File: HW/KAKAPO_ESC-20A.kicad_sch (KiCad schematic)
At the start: 30 parts

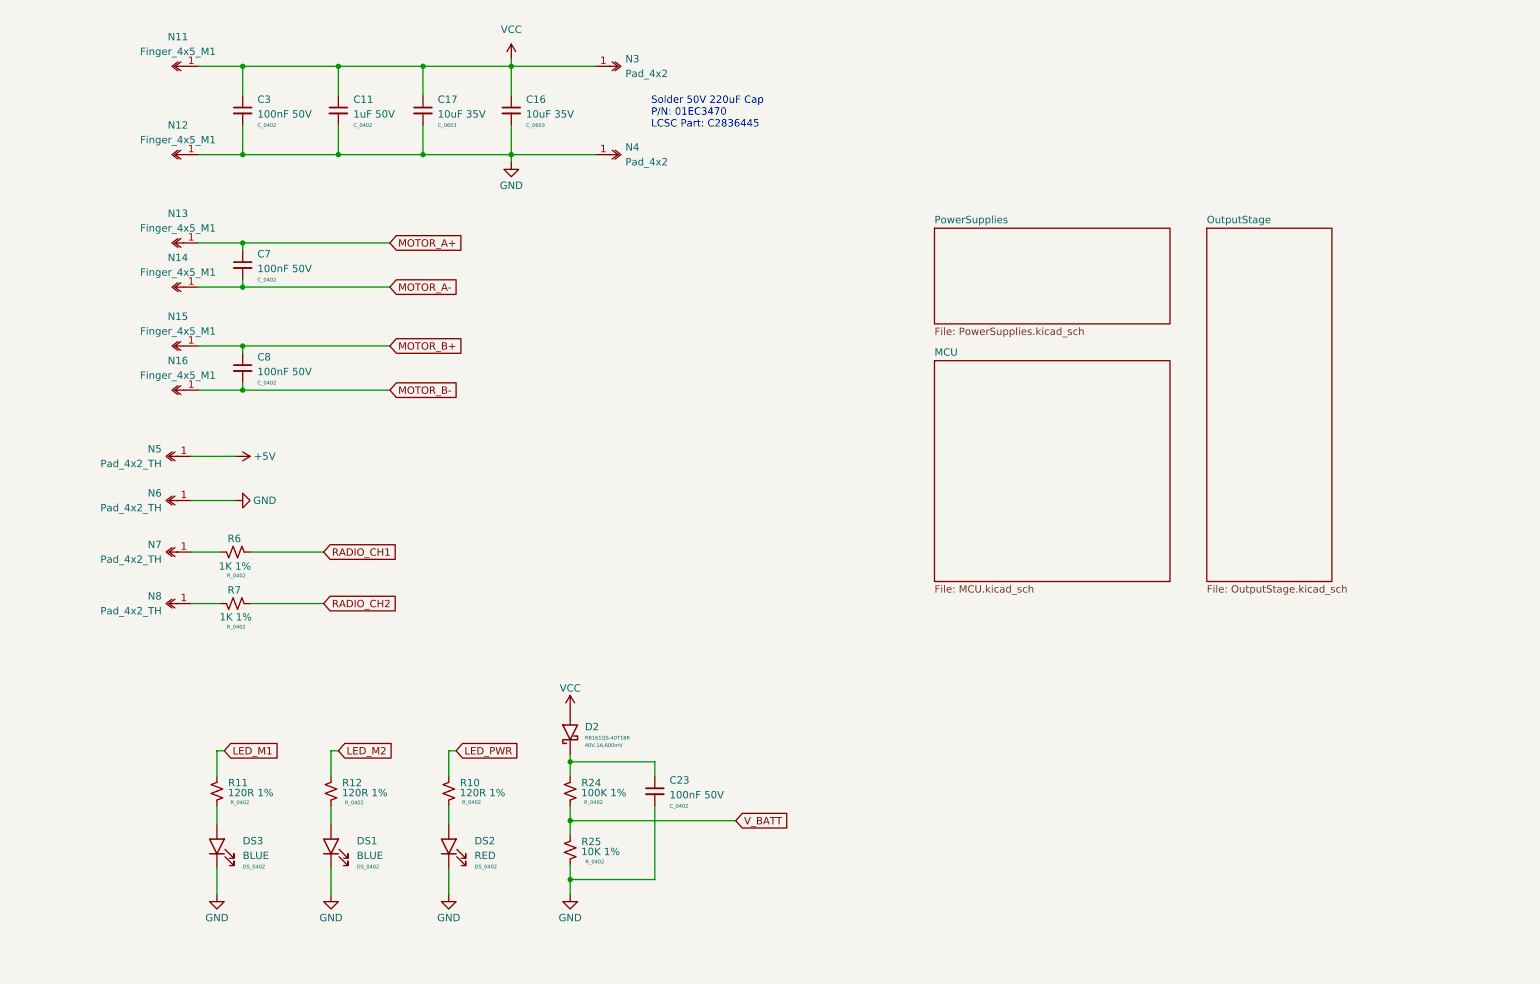
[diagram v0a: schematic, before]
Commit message: WIP - Layout XT30/PCB Finger Positions
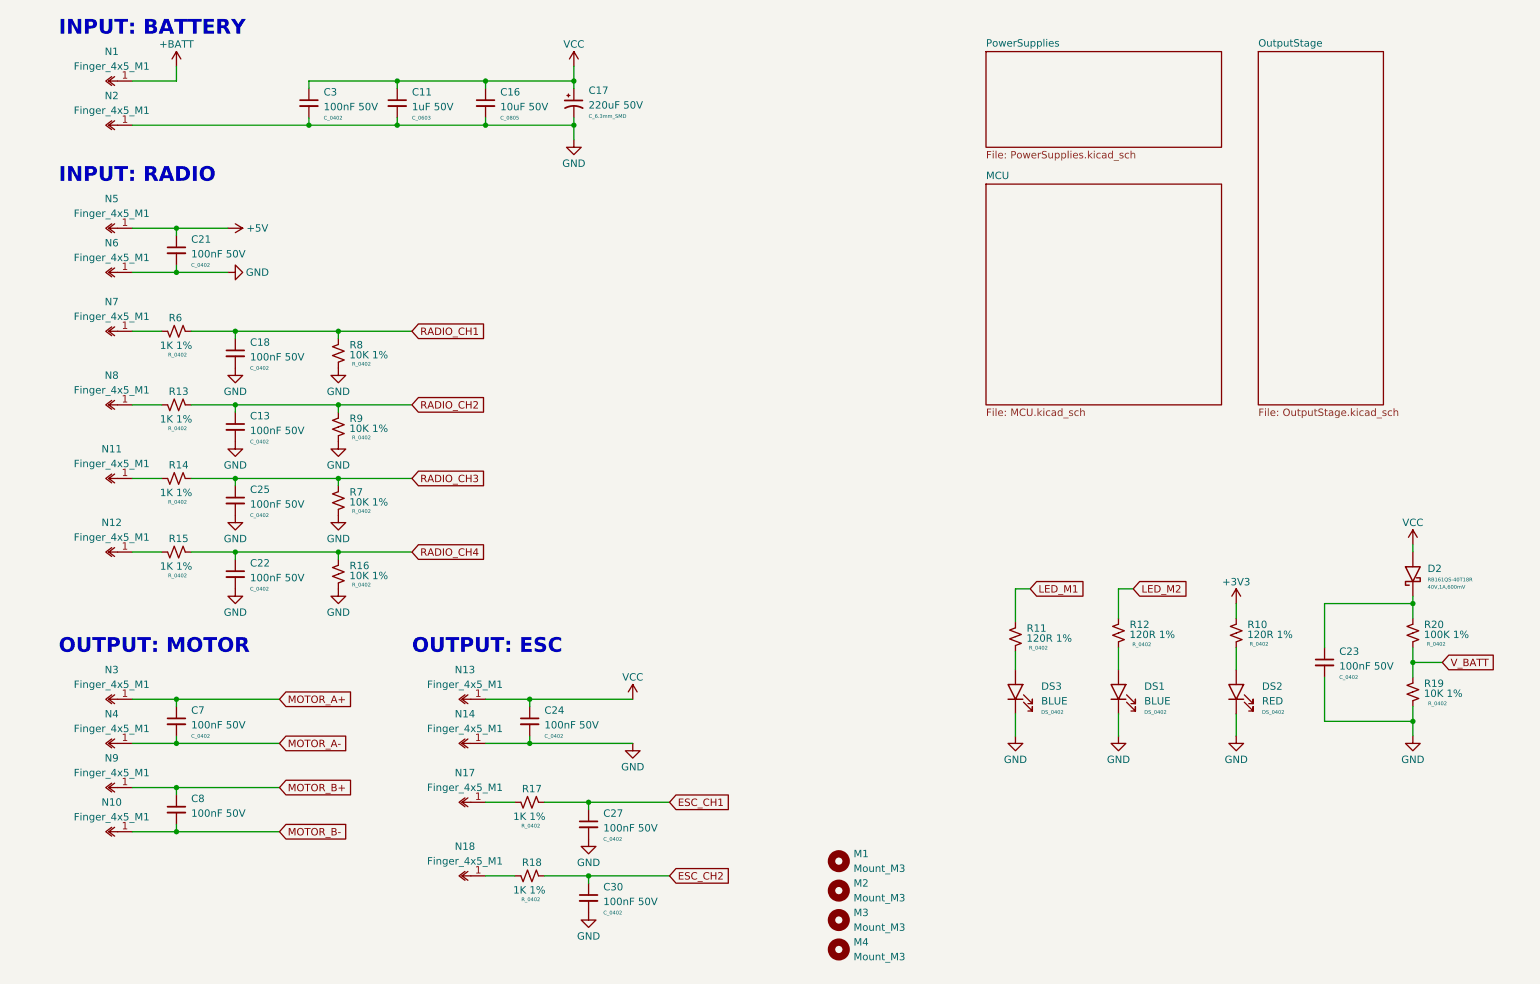
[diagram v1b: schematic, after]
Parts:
- removed C11: 1uF 50V, C_Capacitor:C_0402, symbol C_Capacitor:C_0402
- removed C17: 10uF 35V, C_Capacitor:C_0603, symbol C_Capacitor:C_0805
- removed N15, N16: Finger_4x5_M1, N_NonPart:Finger_4x5_M1, symbol N_NonPart:Finger_4x5_M1
- removed N3, N4: Pad_4x2, N_NonPart:Pad_4x2, symbol N_NonPart:Pad_4x2
- removed N5, N6, N7, N8: Pad_4x2_TH, N_NonPart:Pad_4x2, symbol N_NonPart:Pad_4x2_TH
- removed R24: 100K 1%, R_Resistor:R_0402, symbol R_Resistor:R_0402
- removed R25: 10K 1%, R_Resistor:R_0402, symbol R_Resistor:R_0402
- added C11: 1uF 50V, C_Capacitor:C_0603, symbol C_Capacitor:C_0805
- added C13, C18, C21, C22, C24, C25, C27, C30: 100nF 50V, C_Capacitor:C_0402, symbol C_Capacitor:C_0402
- added C17: 220uF 50V, C_Capacitor:C_6.3mm_SMD, symbol C_Capacitor:C_6.3mm_SMD
- added M1, M2, M3, M4: Mount_M3, M_Mechanical:Mount_M3, symbol M_Mechanical:Mount_M3
- added N1, N10, N17, N18, N2, N3, N4, N5, N6, N7, N8, N9: Finger_4x5_M1, N_NonPart:Finger_4x5_M1, symbol N_NonPart:Finger_4x5_M1
- added R13, R14, R15, R17, R18: 1K 1%, R_Resistor:R_0402, symbol R_Resistor:R_0402
- added R16, R19, R8, R9: 10K 1%, R_Resistor:R_0402, symbol R_Resistor:R_0402
- added R20: 100K 1%, R_Resistor:R_0402, symbol R_Resistor:R_0402
- C16: value 10uF 35V -> 10uF 50V; footprint C_Capacitor:C_0603 -> C_Capacitor:C_0805; LCSC Part C194427 -> (none); Size C_0603 -> C_0805
- R7: value 1K 1% -> 10K 1%; LCSC Part C2935237 -> C309549
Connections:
- net +5V: now also C21.1, N5.1
- net GND: now also N14.1, R7.2, C11.2, C13.2, C17.2, C18.2, C21.2, C22.2, C24.2, C25.2, C27.2, C30.2, N2.1, N6.1, R16.2, R19.2, R8.2, R9.2; no longer N12.1
- net MOTOR_A+: now also N3.1; no longer N13.1
- net MOTOR_A-: now also N4.1; no longer N14.1
- net MOTOR_B+: now also N9.1
- net MOTOR_B-: now also N10.1
- net RADIO_CH1: now also C18.1, R8.1
- net RADIO_CH2: now also C13.1, R13.2, R9.1; no longer R7.2
- net VCC: now also N13.1, C11.1, C17.1, C24.1; no longer N11.1
- net V_BATT: now also R19.1, R20.2
- net RADIO_CH3: now reaches R7.1
- net RADIO_CH3: now also C25.1, R14.2
- net at C23.1, D2.1: now also R20.1
- net at R6.1: now also N7.1
- net LED_PWR renamed +3V3
- new net: N17.1, R17.1
- new net: N12.1, R15.1
- new net: N8.1, R13.1
- new net: N11.1, R14.1
- new net: N18.1, R18.1
- new net +BATT: N1.1
- new net ESC_CH1: C27.1, R17.2
- new net ESC_CH2: C30.1, R18.2
- new net RADIO_CH4: C22.1, R15.2, R16.1
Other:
- note added: "INPUT: BATTERY"
- note added: "INPUT: RADIO"
- note added: "OUTPUT: ESC"
- note added: "OUTPUT: MOTOR"
- note removed: "Solder 50V 220uF Cap P/N: 01EC3470 LCSC Part: C2836445"
- title: WEKA ESC - 20A -> KAKAPO ESC - 20A
- moved on the sheet: DS3, R11, R12

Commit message: WIP - Layout Motor Drivers + Buck Circuit
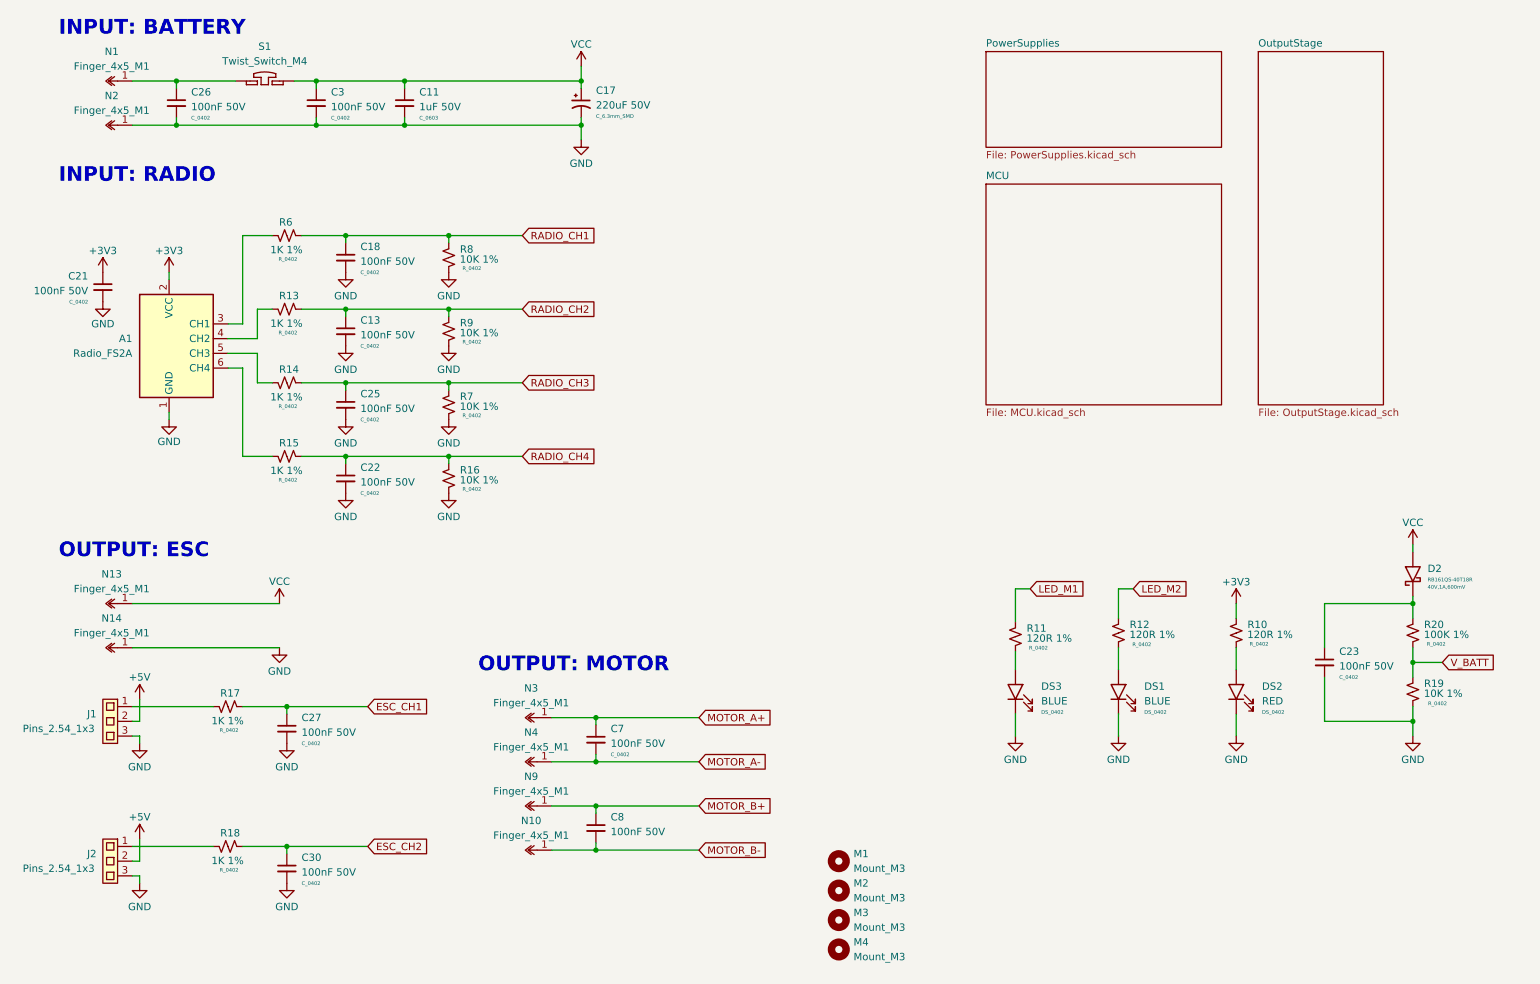
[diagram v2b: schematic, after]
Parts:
- removed C16: 10uF 50V, C_Capacitor:C_0805, symbol C_Capacitor:C_0805
- removed C24: 100nF 50V, C_Capacitor:C_0402, symbol C_Capacitor:C_0402
- removed N11, N12, N17, N18, N5, N6, N7, N8: Finger_4x5_M1, N_NonPart:Finger_4x5_M1, symbol N_NonPart:Finger_4x5_M1
- added A1: Radio_FS2A, A_Assembly:Radio_FS2A, symbol A_Assembly:Radio_FS2A
- added C26: 100nF 50V, C_Capacitor:C_0402, symbol C_Capacitor:C_0402
- added J1, J2: Pins_2.54_1x3, J_Connector:Pins-2.54-1x3, symbol J_Connector:Pins_2.54_1x3
- added S1: Twist_Switch_M4, CombatParts:Twist_Switch_M4, symbol CombatParts:Twist_Switch_M4
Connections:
- net +3V3: now also C21.1, A1.2 (VCC)
- net +5V: now also J1.2, J2.2; no longer C21.1
- net GND: now also A1.1 (GND), C26.2, J1.3, J2.3
- net VCC: now also S1.2
- net at R6.1: now also A1.3 (CH1)
- net at R17.1: now also J1.1
- net at R15.1: now also A1.6 (CH4)
- net at R13.1: now also A1.4 (CH2)
- net at R14.1: now also A1.5 (CH3)
- net at R18.1: now also J2.1
- net +BATT: no longer names the net of N1.1
- net +BATT: now also C26.1, S1.1
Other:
- moved on the sheet: C11, C13, C17, C18, C22, C25, C27, C3, C30, C7, C8, N10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

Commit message: WIP - Continue Tracking MCU
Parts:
- removed C21: 100nF 50V, C_Capacitor:C_0402, symbol C_Capacitor:C_0402
- added C10: 100nF 50V, C_Capacitor:C_0402, symbol C_Capacitor:C_0402
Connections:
- net GND: now also C10.2
- net VCC: now also C10.1
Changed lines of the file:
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@@
   (junction (at 62.23 170.18) (diameter 0) (color 0 0 0 0)
   )
+  (junction (at 43.18 135.89) (diameter 0) (color 0 0 0 0)
+  )
   (junction (at 90.17 90.17) (diameter 0) (color 0 0 0 0)
   )
@@
   (junction (at 72.39 102.87) (diameter 0) (color 0 0 0 0)
   )
+  (junction (at 43.18 128.27) (diameter 0) (color 0 0 0 0)
+  )
   (junction (at 256.54 148.59) (diameter 0) (color 0 0 0 0)
   )
@@
     (stroke (width 0) (type default))
   )
+  (wire (pts (xy 43.18 134.62) (xy 43.18 135.89))
+    (stroke (width 0) (type default))
+  )
   (wire (pts (xy 62.23 171.45) (xy 62.23 170.18))
     (stroke (width 0) (type default))
@@
     (stroke (width 0) (type default))
   )
+  (wire (pts (xy 43.18 128.27) (xy 43.18 129.54))
+    (stroke (width 0) (type default))
+  )
   (wire (pts (xy 54.61 64.77) (xy 59.69 64.77))
     (stroke (width 0) (type default))
@@
     (stroke (width 0) (type default))
   )
-  (wire (pts (xy 35.56 135.89) (xy 60.96 135.89))
+  (wire (pts (xy 35.56 135.89) (xy 43.18 135.89))
     (stroke (width 0) (type default))
   )
@@
     (stroke (width 0) (type default))
   )
+  (wire (pts (xy 43.18 135.89) (xy 60.96 135.89))
+    (stroke (width 0) (type default))
+  )
   (wire (pts (xy 107.95 170.815) (xy 115.57 170.815))
     (stroke (width 0) (type default))
@@
     (stroke (width 0) (type default))
   )
-  (wire (pts (xy 35.56 128.27) (xy 60.96 128.27))
+  (wire (pts (xy 35.56 128.27) (xy 43.18 128.27))
     (stroke (width 0) (type default))
   )
@@
     (stroke (width 0) (type default))
   )
+  (wire (pts (xy 43.18 128.27) (xy 60.96 128.27))
+    (stroke (width 0) (type default))
+  )
   (wire (pts (xy 72.39 77.47) (xy 90.17 77.47))
     (stroke (width 0) (type default))
@@
     )
   )
-  (symbol (lib_id "C_Capacitor:C_0402") (at 30.48 73.66 0) (mirror y) (unit 1)
-    (in_bom yes) (on_board yes) (dnp no)
-    (property "Reference" "C21" (at 27.94 71.7613 0)
-      (effects (font (size 1.27 1.27)) (justify left))
-    )
-    (property "Value" "100nF 50V" (at 27.94 74.3013 0)
-      (effects (font (size 1.27 1.27)) (justify left))
-    )
-    (property "Footprint" "C_Capacitor:C_0402" (at 33.655 73.66 90)
-      (effects (font (size 1.27 1.27)) hide)
-    )
-    (property "Datasheet" "" (at 27.94 71.12 0)
-      (effects (font (size 1.27 1.27)) hide)
-    )
-    (property "Size" "C_0402" (at 27.94 76.2063 0)
-      (effects (font (size 0.635 0.635)) (justify left))
-    )
-    (property "LCSC Part" "C105882" (at 30.48 73.66 0)
-      (effects (font (size 1.27 1.27)) hide)
-    )
-    (pin "1")
-    (pin "2")
-    (instances
-      (project "KAKAPO_ESC-20A"
-        (path "/e63e39d7-6ac0-4ffd-8aa3-1841a4541b55"
-          (reference "C21") (unit 1)
-        )
-      )
-    )
-  )
   (symbol (lib_id "R_Resistor:R_0402") (at 205.74 133.35 0) (mirror y) (unit 1)
     (in_bom yes) (on_board yes) (dnp no)
@@
     )
   )
+  (symbol (lib_id "C_Capacitor:C_0402") (at 43.18 132.08 0) (unit 1)
+    (in_bom yes) (on_board yes) (dnp no) (fields_autoplaced)
+    (property "Reference" "C10" (at 45.72 130.1813 0)
+      (effects (font (size 1.27 1.27)) (justify left))
+    )
+    (property "Value" "100nF 50V" (at 45.72 132.7213 0)
+      (effects (font (size 1.27 1.27)) (justify left))
+    )
+    (property "Footprint" "C_Capacitor:C_0402" (at 40.005 132.08 90)
+      (effects (font (size 1.27 1.27)) hide)
+    )
+    (property "Datasheet" "" (at 45.72 129.54 0)
+      (effects (font (size 1.27 1.27)) hide)
+    )
+    (property "Size" "C_0402" (at 45.72 134.6263 0)
+      (effects (font (size 0.635 0.635)) (justify left))
+    )
+    (property "LCSC Part" "C105882" (at 43.18 132.08 0)
+      (effects (font (size 1.27 1.27)) hide)
+    )
+    (pin "1")
+    (pin "2")
+    (instances
+      (project "KAKAPO_ESC-20A"
+        (path "/e63e39d7-6ac0-4ffd-8aa3-1841a4541b55"
+          (reference "C10") (unit 1)
+        )
+      )
+    )
+  )
   (symbol (lib_id "A_Assembly:Radio_FS2A") (at 36.83 92.71 0) (unit 1)
     (in_bom yes) (on_board yes) (dnp no) (fields_autoplaced)
@@
         )
       )
-    )
-  )
-  (symbol (lib_id "power:+3V3") (at 30.48 71.12 0) (unit 1)
-    (in_bom yes) (on_board yes) (dnp no)
-    (property "Reference" "#PWR05" (at 30.48 74.93 0)
-      (effects (font (size 1.27 1.27)) hide)
-    )
-    (property "Value" "+3V3" (at 30.48 67.3862 0)
-      (effects (font (size 1.27 1.27)))
-    )
-    (property "Footprint" "" (at 30.48 71.12 0)
-      (effects (font (size 1.27 1.27)) hide)
-    )
-    (property "Datasheet" "" (at 30.48 71.12 0)
-      (effects (font (size 1.27 1.27)) hide)
-    )
-    (pin "1")
-    (instances
-      (project "KAKAPO_ESC-20A"
-        (path "/e63e39d7-6ac0-4ffd-8aa3-1841a4541b55"
-          (reference "#PWR05") (unit 1)
-        )
-      )
-    )
-  )
-  (symbol (lib_name "GND_2") (lib_id "power:GND") (at 30.48 76.2 0) (mirror y) (unit 1)
-    (in_bom yes) (on_board yes) (dnp no)
-    (property "Reference" "#PWR037" (at 30.48 82.55 0)
-      (effects (font (size 1.27 1.27)) hide)
-    )
-    (property "Value" "GND" (at 30.48 80.01 0)
-      (effects (font (size 1.27 1.27)))
-    )
-    (property "Footprint" "" (at 30.48 76.2 0)
-      (effects (font (size 1.27 1.27)) hide)
-    )
-    (property "Datasheet" "" (at 30.48 76.2 0)
-      (effects (font (size 1.27 1.27)) hide)
-    )
-    (pin "1")
-    (instances
-      (project "KAKAPO_ESC-20A"
-        (path "/e63e39d7-6ac0-4ffd-8aa3-1841a4541b55"
-          (reference "#PWR037") (unit 1)
-        )
-      )

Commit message: WIP - Final Detail Design Before Design Review
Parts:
- removed C11: 1uF 50V, C_Capacitor:C_0603, symbol C_Capacitor:C_0805
- removed C3: 100nF 50V, C_Capacitor:C_0402, symbol C_Capacitor:C_0402
- removed DS2: RED, DS_LED:DS_0402, symbol DS_LED:DS_0402
- removed R10: 120R 1%, R_Resistor:R_0402, symbol R_Resistor:R_0402
- added DS2: RED, DS_LED:DS_Everlight_IR21-21CL110TR8, symbol DS_LED:DS_IR21-21CL110TR8
- added R24: 1K 1%, R_Resistor:R_1206, symbol R_Resistor:R_1206
- C13, C18, C22, C25: value 100nF 50V -> 1nF 50V
- R16, R7, R8, R9: now not fitted
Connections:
- net GND: now also DS2.1 (K)
- net VCC: now also S1.1, R24.1; no longer S1.2
- net at C26.1, N1.1: now also S1.2; no longer S1.1
- new net: DS2.2 (A), R24.2
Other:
- moved on the sheet: C17
